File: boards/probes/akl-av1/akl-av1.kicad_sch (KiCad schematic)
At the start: 28 parts, among them J2 TIPRES, J3 TIPRES, J4 SMPM, U4 BUF802, U5 ADA4075-2

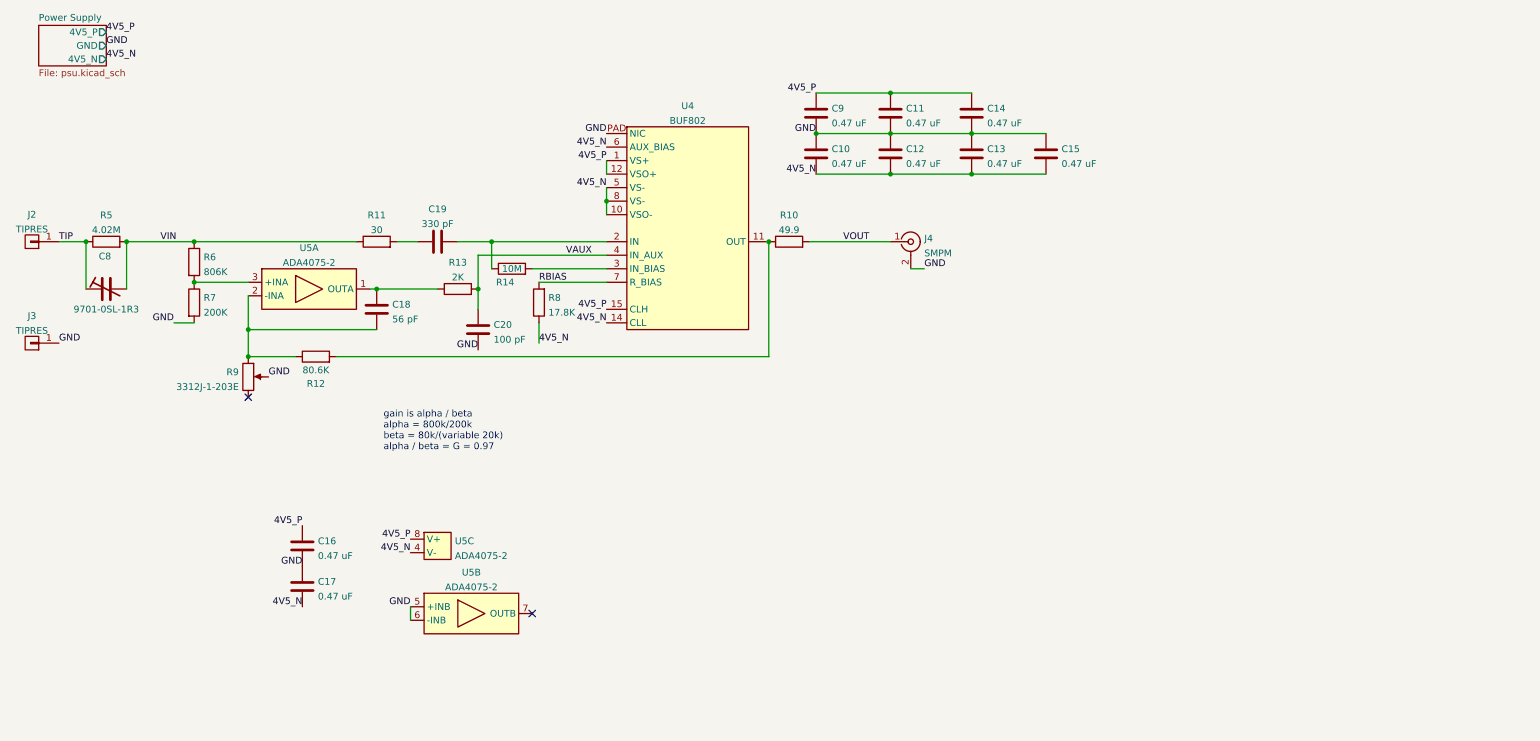
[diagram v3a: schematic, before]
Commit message: Updated AKL-AV1 with v0.4 layout including OPA210 and noise filter
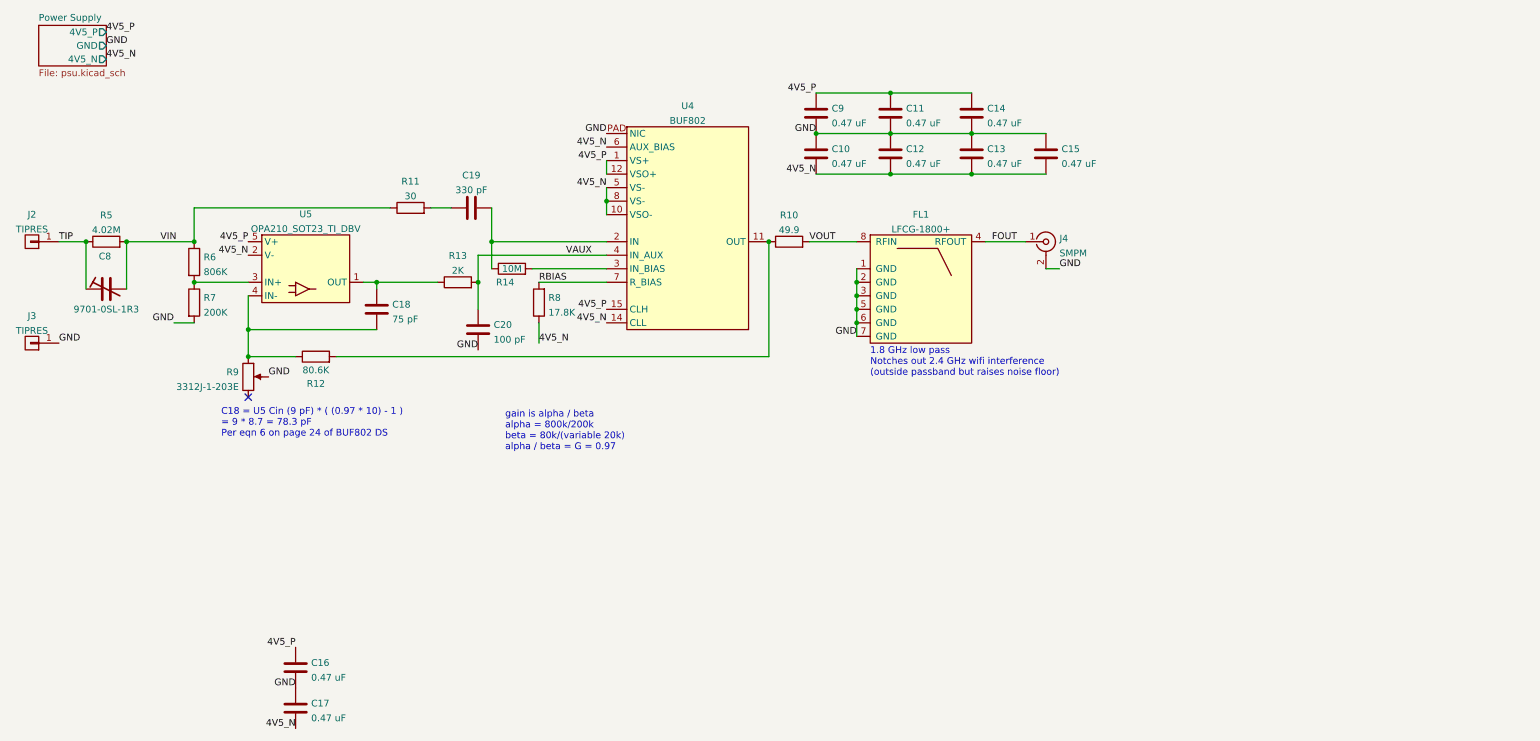
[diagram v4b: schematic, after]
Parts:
- removed U5: ADA4075-2, azonenberg_pcb:DFN_8_0.5MM_2x2MM_NOPAD, symbol analog-azonenberg:ADA4075-2
- added FL1: LFCG-1800+, azonenberg_pcb:FILTER_MINICIRCUITS_LFCG, symbol analog-azonenberg:FILTER_MINICIRCUITS_LFCG
- added U5: OPA210_SOT23_TI_DBV, azonenberg_pcb:SOT23_5, symbol analog-azonenberg:OPA210_SOT23_TI_DBV
- C18: value 56 pF -> 75 pF
- J4: footprint azonenberg_pcb:CONN_SMPM_AMPHENOL_925-169J-51PT -> azonenberg_pcb:CONN_SMPM_AMPHENOL_925-169J-51PT_SHORT
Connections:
- net 4V5_N: now also U5.2 (V-)
- net 4V5_P: now also U5.5 (V+)
- net GND: now also FL1.1 (GND), FL1.2 (GND), FL1.3 (GND), FL1.5 (GND), FL1.6 (GND), FL1.7 (GND)
- net VOUT: now also FL1.8 (RFIN); no longer J4.1 (In)
- net at C18.1, R12.1, R9.1: now also U5.4 (IN-)
- net at C18.2, R13.1: now also U5.1 (OUT)
- net at R6.2, R7.1: now also U5.3 (IN+)
- new net FOUT: FL1.4 (RFOUT), J4.1 (In)
- no-connect marks 2 -> 1
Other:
- note added: "1.8 GHz low pass Notches out 2.4 GHz wifi interference (outside passband but raises noise floor)"
- note added: "C18 = U5 Cin (9 pF) * ( (0.97 * 10) - 1 ) = 9 * 8.7 = 78.3 pF Per eqn 6 on page 24 of BUF802 DS"
- company: (none) -> Antikernel Labs
- title: (none) -> AKL-AV1 High Impedance Active Voltage Probe
- moved on the sheet: C16, C17, C19, J4, R11, R13

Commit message: AKL-AV1 v0.5 with new power supply, GSG tip, clearance fixes, and passive CTLE
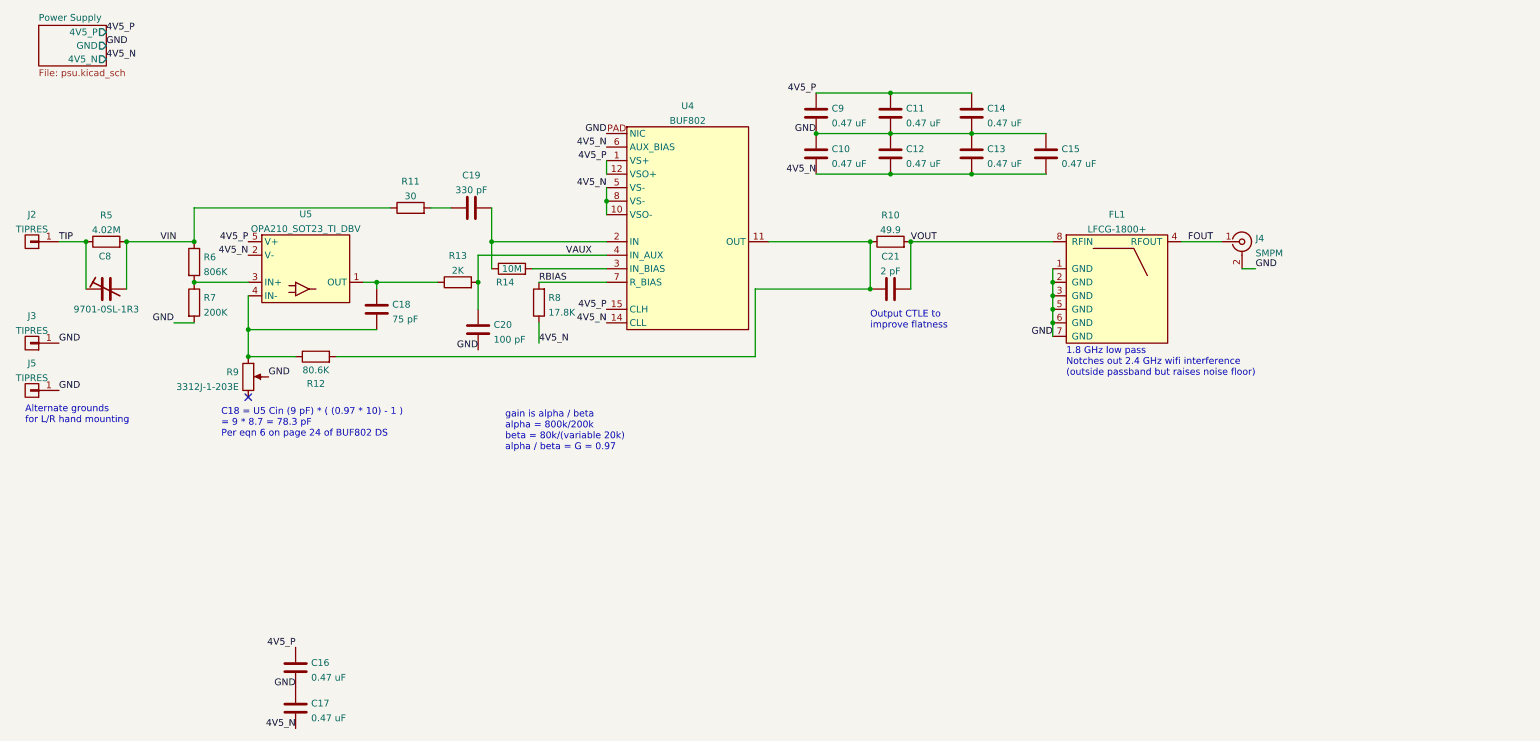
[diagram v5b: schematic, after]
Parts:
- added C21: 2 pF, azonenberg_pcb:EIA_0402_CAP_NOSILK, symbol device:C
- added J5: TIPRES, azonenberg_pcb:EDGELAUNCH_350UM, symbol conn:CONN_01X01
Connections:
- net GND: now also J5.1 (P1)
- net VOUT: now also C21.2
- net at R10.1, R12.2, U4.11 (OUT): now also C21.1
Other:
- note added: "Alternate grounds for L/R hand mounting"
- note added: "Output CTLE to improve flatness"
- moved on the sheet: FL1, J4, R10

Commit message: Updated AKL-AV1 to v0.6
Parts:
- removed FL1: LFCG-1800+, azonenberg_pcb:FILTER_MINICIRCUITS_LFCG, symbol analog-azonenberg:FILTER_MINICIRCUITS_LFCG
- added C22: GJM1555C1H4R0WB01D, azonenberg_pcb:EIA_0402_CAP_NOSILK, symbol device:C
- added C7: GJM1555C1H1R1WB01D, azonenberg_pcb:EIA_0402_CAP_NOSILK, symbol device:C
- added L1: LQG15HN1N0S02D, azonenberg_pcb:EIA_0402_CAP_NOSILK, symbol device:L
- added L2: LQG15HN4N7C02D, azonenberg_pcb:EIA_0402_CAP_NOSILK, symbol device:L
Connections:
- net FOUT: now also C22.2, L2.1
- net GND: now also C22.1, C7.1
- net VOUT: now also L1.2
- new net: C7.2, L1.1, L2.2
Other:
- note added: "100 ohm Vishay HML from DUT to J2 Ground lead from DUT to J3 or J5"
- note added: "4th order Bessel LPF 1.8 GHz design cutoff"
- note removed: "1.8 GHz low pass Notches out 2.4 GHz wifi interference (outside passband but raises noise floor)"
- moved on the sheet: J4

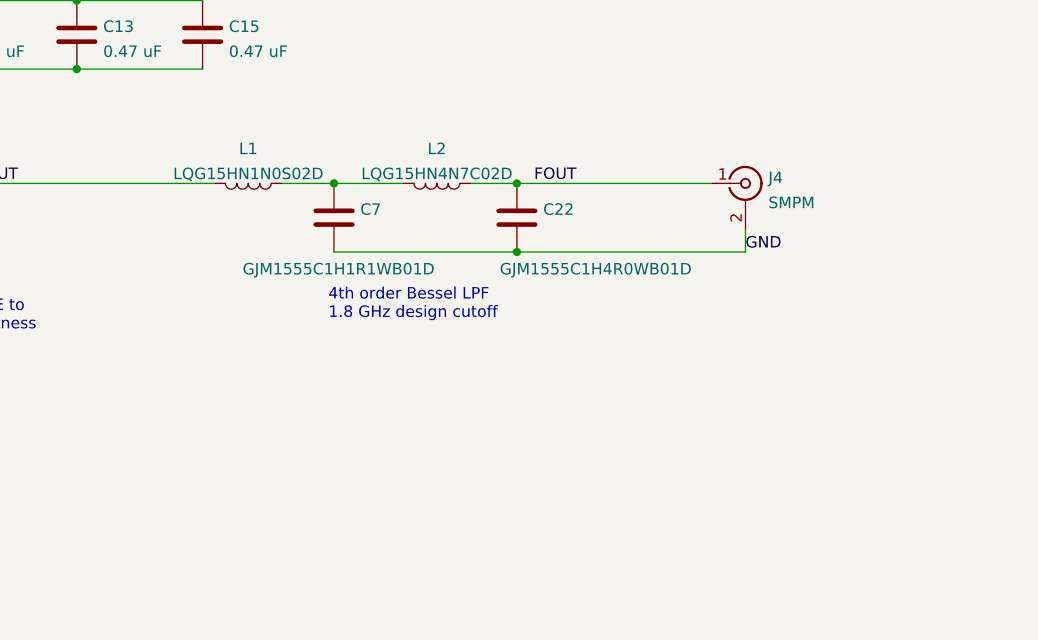
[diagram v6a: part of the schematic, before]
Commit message: AKL-AV1: updated passives for new filter
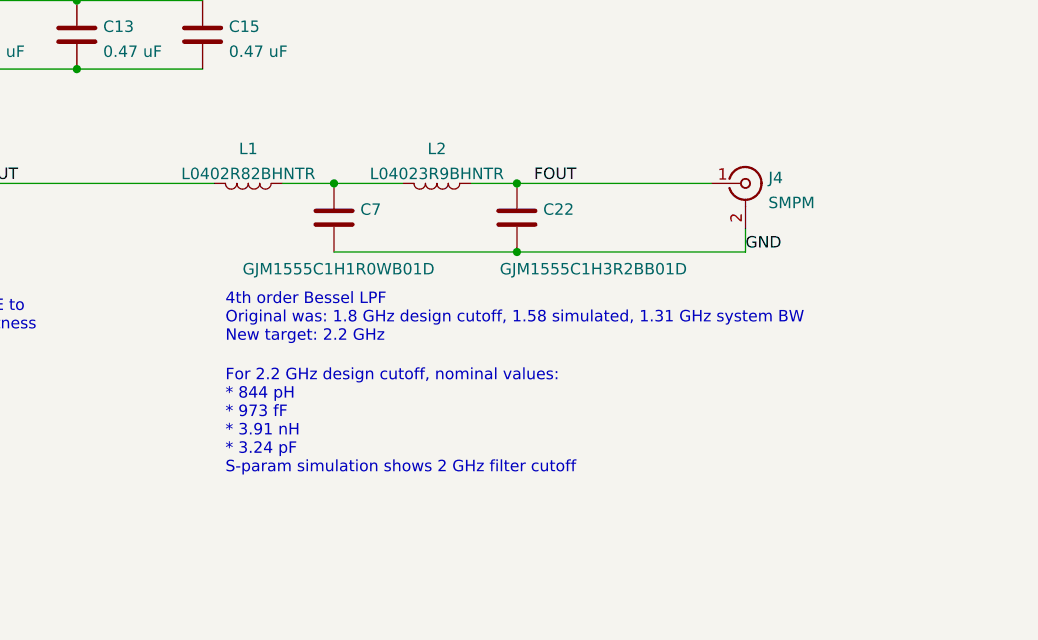
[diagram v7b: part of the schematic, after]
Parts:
- C22: value GJM1555C1H4R0WB01D -> GJM1555C1H3R2BB01D
- C7: value GJM1555C1H1R1WB01D -> GJM1555C1H1R0WB01D
- L1: value LQG15HN1N0S02D -> L0402R82BHNTR
- L2: value LQG15HN4N7C02D -> L04023R9BHNTR
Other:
- note added: "4th order Bessel LPF Original was: 1.8 GHz design cutoff, 1.58 simulated, 1.31 GHz system BW New target: 2.2 GHz"
- note added: "For 2.2 GHz design cutoff, nominal values: * 844 pH * 973 fF * 3.91 nH * 3.24 pF S-param simulation shows 2 GHz filter cutoff"
- note removed: "4th order Bessel LPF 1.8 GHz design cutoff"
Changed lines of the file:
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@@
     (effects (font (size 1.27 1.27)) (justify left bottom))
   )
-  (text "4th order Bessel LPF\n1.8 GHz design cutoff" (at 220.98 74.93 0)
+  (text "4th order Bessel LPF\nOriginal was: 1.8 GHz design cutoff, 1.58 simulated, 1.31 GHz system BW\nNew target: 2.2 GHz"
+    (at 209.55 77.47 0)
     (effects (font (size 1.27 1.27)) (justify left bottom))
   )
   (text "100 ohm Vishay HML from DUT to J2\nGround lead from DUT to J3 or J5 "
     (at 13.97 50.8 0)
+    (effects (font (size 1.27 1.27)) (justify left bottom))
+  )
+  (text "For 2.2 GHz design cutoff, nominal values:\n* 844 pH\n* 973 fF\n* 3.91 nH\n* 3.24 pF\nS-param simulation shows 2 GHz filter cutoff"
+    (at 209.55 92.075 0)
     (effects (font (size 1.27 1.27)) (justify left bottom))
   )
@@
       (effects (font (size 1.27 1.27)) (justify right))
     )
-    (property "Value" "GJM1555C1H1R1WB01D" (id 1) (at 211.455 69.215 0)
+    (property "Value" "GJM1555C1H1R0WB01D" (id 1) (at 211.455 69.215 0)
       (effects (font (size 1.27 1.27)) (justify right))
     )
@@
     (in_bom yes) (on_board yes) (fields_autoplaced)
     (property "Reference" "L2" (id 0) (at 233.045 55.8505 90))
-    (property "Value" "LQG15HN4N7C02D" (id 1) (at 233.045 58.6256 90))
+    (property "Value" "L04023R9BHNTR" (id 1) (at 233.045 58.6256 90))
     (property "Footprint" "azonenberg_pcb:EIA_0402_CAP_NOSILK" (id 2) (at 233.045 59.69 0)
       (effects (font (size 1.27 1.27)) hide)
@@
     (in_bom yes) (on_board yes) (fields_autoplaced)
     (property "Reference" "L1" (id 0) (at 212.09 55.8505 90))
-    (property "Value" "LQG15HN1N0S02D" (id 1) (at 212.09 58.6256 90))
+    (property "Value" "L0402R82BHNTR" (id 1) (at 212.09 58.6256 90))
     (property "Footprint" "azonenberg_pcb:EIA_0402_CAP_NOSILK" (id 2) (at 212.09 59.69 0)
       (effects (font (size 1.27 1.27)) hide)
@@
       (effects (font (size 1.27 1.27)) (justify right))
     )
-    (property "Value" "GJM1555C1H4R0WB01D" (id 1) (at 240.03 69.215 0)
+    (property "Value" "GJM1555C1H3R2BB01D" (id 1) (at 240.03 69.215 0)
       (effects (font (size 1.27 1.27)) (justify right))
     )
@@
     )
     (path "/2a72d102-5cc2-46a5-ba1d-7fad5fd13e56"
-      (reference "C7") (unit 1) (value "GJM1555C1H1R1WB01D") (footprint "azonenberg_pcb:EIA_0402_CAP_NOSILK")
+      (reference "C7") (unit 1) (value "GJM1555C1H1R0WB01D") (footprint "azonenberg_pcb:EIA_0402_CAP_NOSILK")
     )
     (path "/bd065bd8-f096-4339-86bc-73022c7c9598"
@@
     )
     (path "/d3beebe0-c3be-42e7-b903-8d54a7dd6e53"
-      (reference "C22") (unit 1) (value "GJM1555C1H4R0WB01D") (footprint "azonenberg_pcb:EIA_0402_CAP_NOSILK")
+      (reference "C22") (unit 1) (value "GJM1555C1H3R2BB01D") (footprint "azonenberg_pcb:EIA_0402_CAP_NOSILK")
     )
     (path "/a12b751e-ae7a-468c-af3d-31ed4d501b01/b2ee61e9-2ecc-4e69-9c1a-3d3d2b7bee7d"
@@
     )
     (path "/ca1af6e0-b911-4719-a936-e41d586110b5"
-      (reference "L1") (unit 1) (value "LQG15HN1N0S02D") (footprint "azonenberg_pcb:EIA_0402_CAP_NOSILK")
+      (reference "L1") (unit 1) (value "L0402R82BHNTR") (footprint "azonenberg_pcb:EIA_0402_CAP_NOSILK")
     )
     (path "/95d3d7e1-641f-435c-9cc8-0d359ea2fc7b"
-      (reference "L2") (unit 1) (value "LQG15HN4N7C02D") (footprint "azonenberg_pcb:EIA_0402_CAP_NOSILK")
+      (reference "L2") (unit 1) (value "L04023R9BHNTR") (footprint "azonenberg_pcb:EIA_0402_CAP_NOSILK")
     )
     (path "/a12b751e-ae7a-468c-af3d-31ed4d501b01/26c9a61b-49de-43ad-b3c9-7b4385b6b4c9"
